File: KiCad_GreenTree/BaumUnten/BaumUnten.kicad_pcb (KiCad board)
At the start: 2 copper layers, 73.4 x 96.9 mm, 44 parts

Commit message: sterne auf silkscreen baum
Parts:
- added G***: LOGO, grafics:star_silk, B.Cu at (103.9, 60.4)
- added G***: LOGO, grafics:star_silk, B.Cu at (85.9, 110.4)
- added G***: LOGO, grafics:star_silk, B.Cu at (105.0, 108.2)
- added G***: LOGO, grafics:star_silk, B.Cu at (77.6, 128.6)
- added G***: LOGO, grafics:star_silk, B.Cu at (113.8, 131.1)
- added G***: LOGO, grafics:star_silk, B.Cu at (119.2, 112.6)
- added G***: LOGO, grafics:star_silk, B.Cu at (108.3, 117.4)
- added G***: LOGO, grafics:star_silk, B.Cu at (132.0, 124.4)
- added G***: LOGO, grafics:star_silk, F.Cu at (110.8, 106.9)
- added G***: LOGO, grafics:star_silk, F.Cu at (116.5, 92.4)
- added G***: LOGO, grafics:star_silk, F.Cu at (108.7, 73.5)
- added G***: LOGO, grafics:star_silk, B.Cu at (88.7, 73.4)
- added G***: LOGO, grafics:star_silk, F.Cu at (106.8, 95.9)
- added G***: LOGO, grafics:star_silk, F.Cu at (106.4, 121.0)
- added G***: LOGO, grafics:star_silk, F.Cu at (123.3, 127.4)
- added G***: LOGO, grafics:star_silk, F.Cu at (91.3, 125.0)
- added G***: LOGO, grafics:star_silk, F.Cu at (79.9, 115.0)
- added G***: LOGO, grafics:star_silk, F.Cu at (71.8, 124.6)
- added G***: LOGO, grafics:star_silk, F.Cu at (104.1, 85.2)
- added G***: LOGO, grafics:star_silk, F.Cu at (96.4, 104.0)
- added G***: LOGO, grafics:star_silk, F.Cu at (88.0, 95.2)
- added G***: LOGO, grafics:star_silk, F.Cu at (87.4, 86.9)
- added G***: LOGO, grafics:star_silk, B.Cu at (93.5, 85.8)
- added G***: LOGO, grafics:star_silk, F.Cu at (97.0, 75.8)
- added G***: LOGO, grafics:star_silk, F.Cu at (93.5, 68.9)
- added G***: LOGO, grafics:star_silk, F.Cu at (97.5, 61.4)
- added G***: LOGO, grafics:star_silk, B.Cu at (111.8, 87.6)
- added G***: LOGO, grafics:star_silk, B.Cu at (87.3, 87.7)
- added G***: LOGO, grafics:star_silk, B.Cu at (79.3, 98.5)
- added G***: LOGO, grafics:star_silk, B.Cu at (110.5, 70.6)
- added G***: LOGO, grafics:star_silk, B.Cu at (92.0, 99.9)
- added G***: LOGO, grafics:star_silk, B.Cu at (125.1, 99.5)
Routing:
- net Net-(DG2-Pad1): track 44.1 -> 44.7 mm
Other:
- board size 73.4 x 96.9 mm -> 73.4 x 97.1 mm

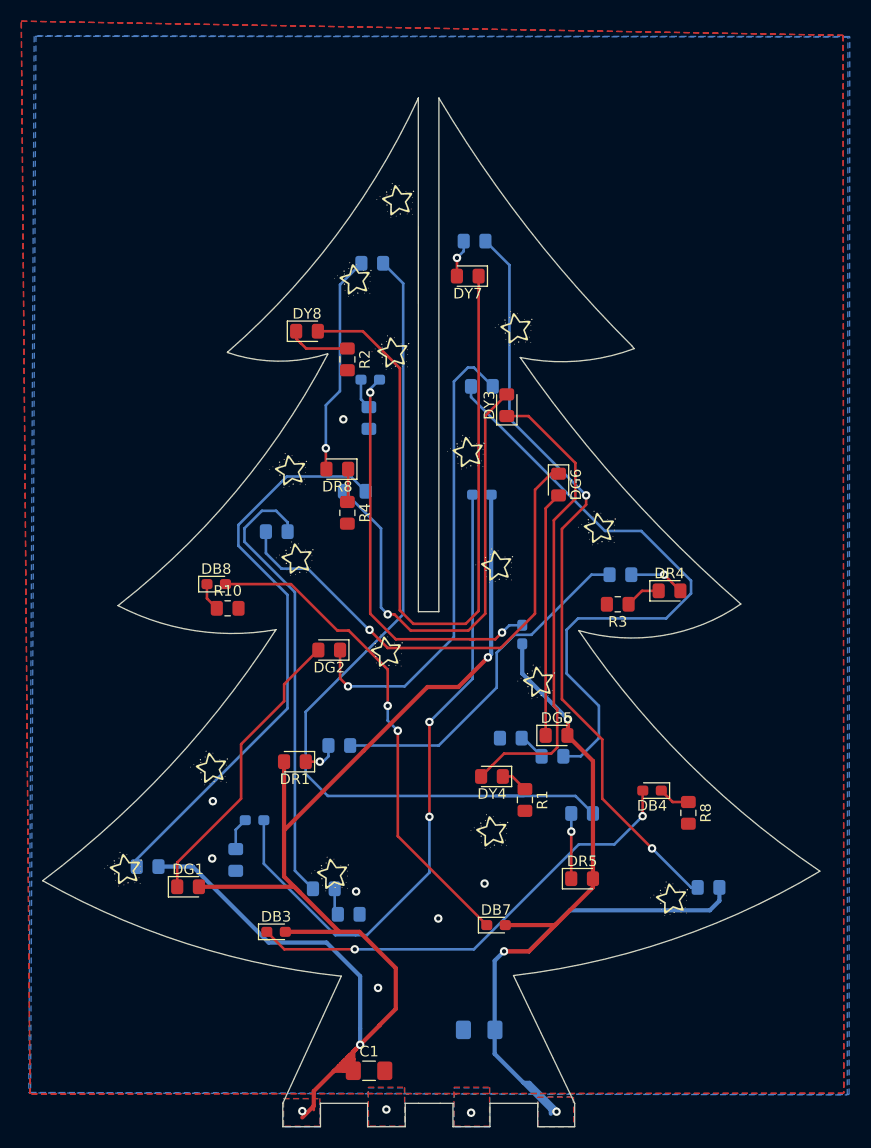
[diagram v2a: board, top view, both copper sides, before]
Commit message: edgecuts angepasst
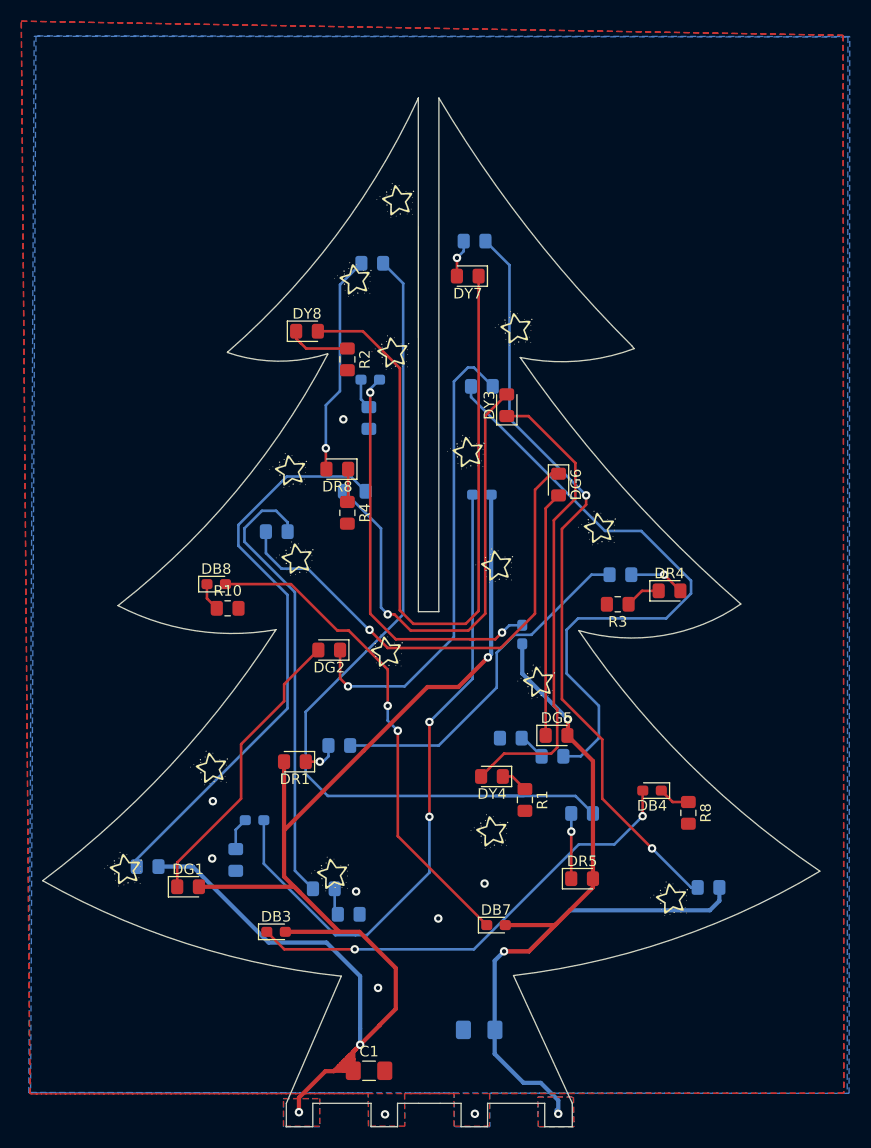
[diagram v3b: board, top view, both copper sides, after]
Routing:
- net Takt_invertiert_9V: track 87.5 -> 84.5 mm
- net Takt_9V: track 143.7 -> 142.0 mm
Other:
- outline, holes or cut-outs redrawn
